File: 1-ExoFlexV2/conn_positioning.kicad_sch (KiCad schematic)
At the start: 39 parts, among them J47 3, J48 3, J49 3, J50 2, J51 2, J52 2, J53 4, J54 4, J55 4

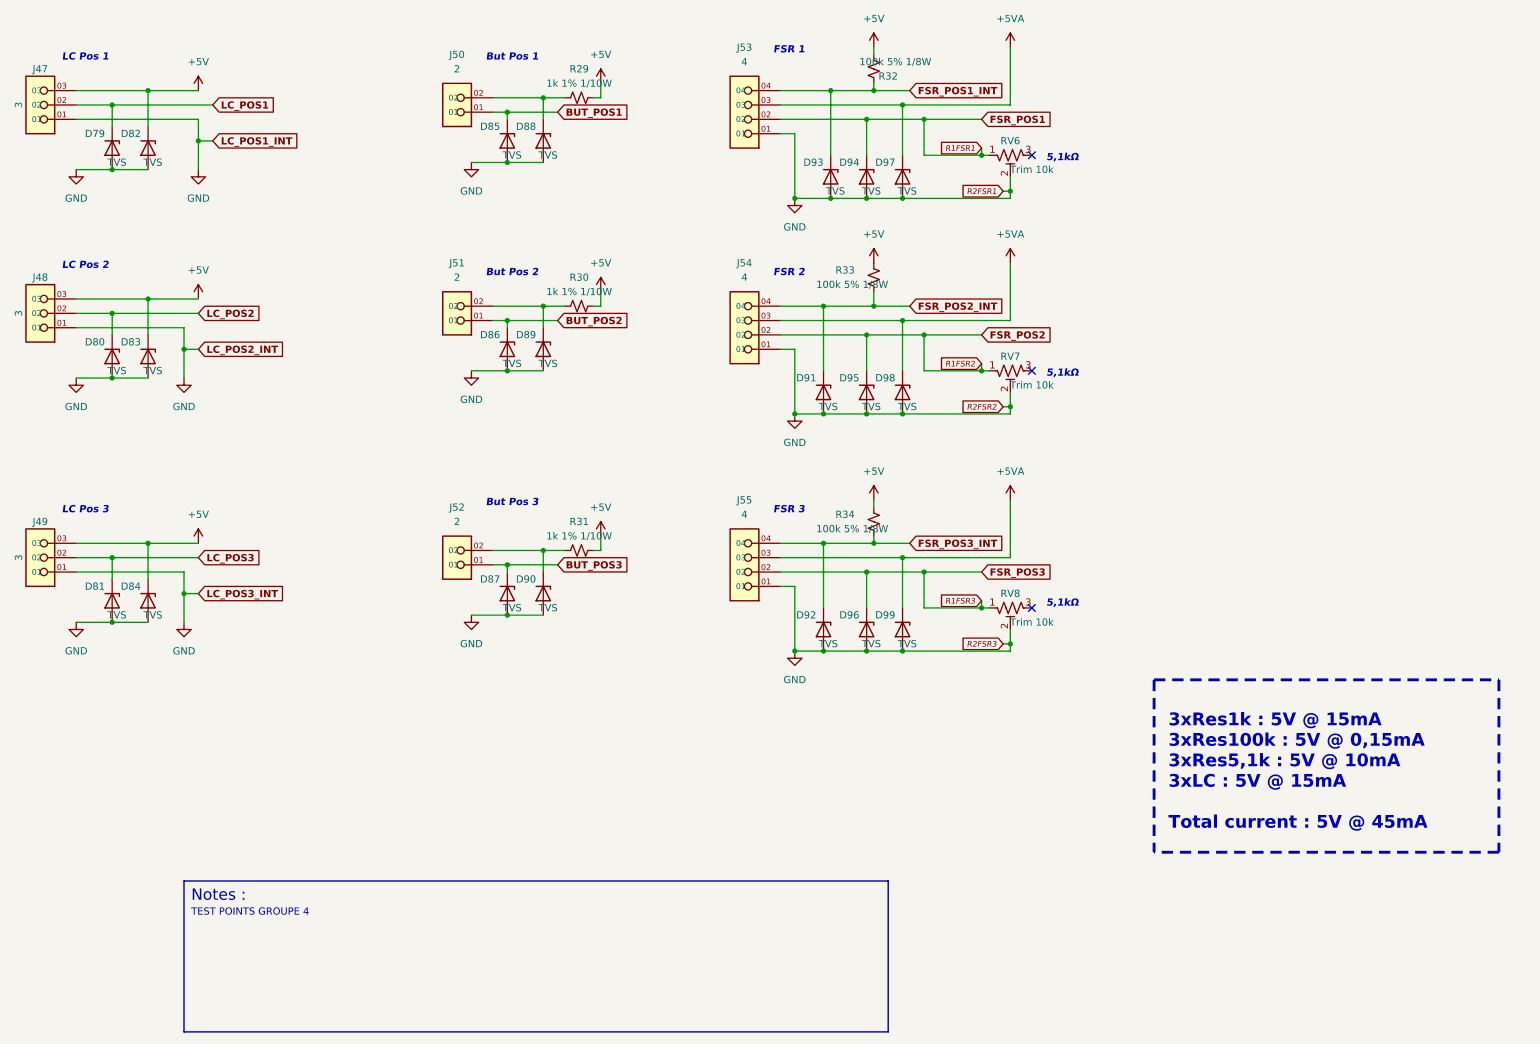
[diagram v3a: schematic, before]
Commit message: Bug NetList
- Ajout de net-tie pour les GND et et les +5V
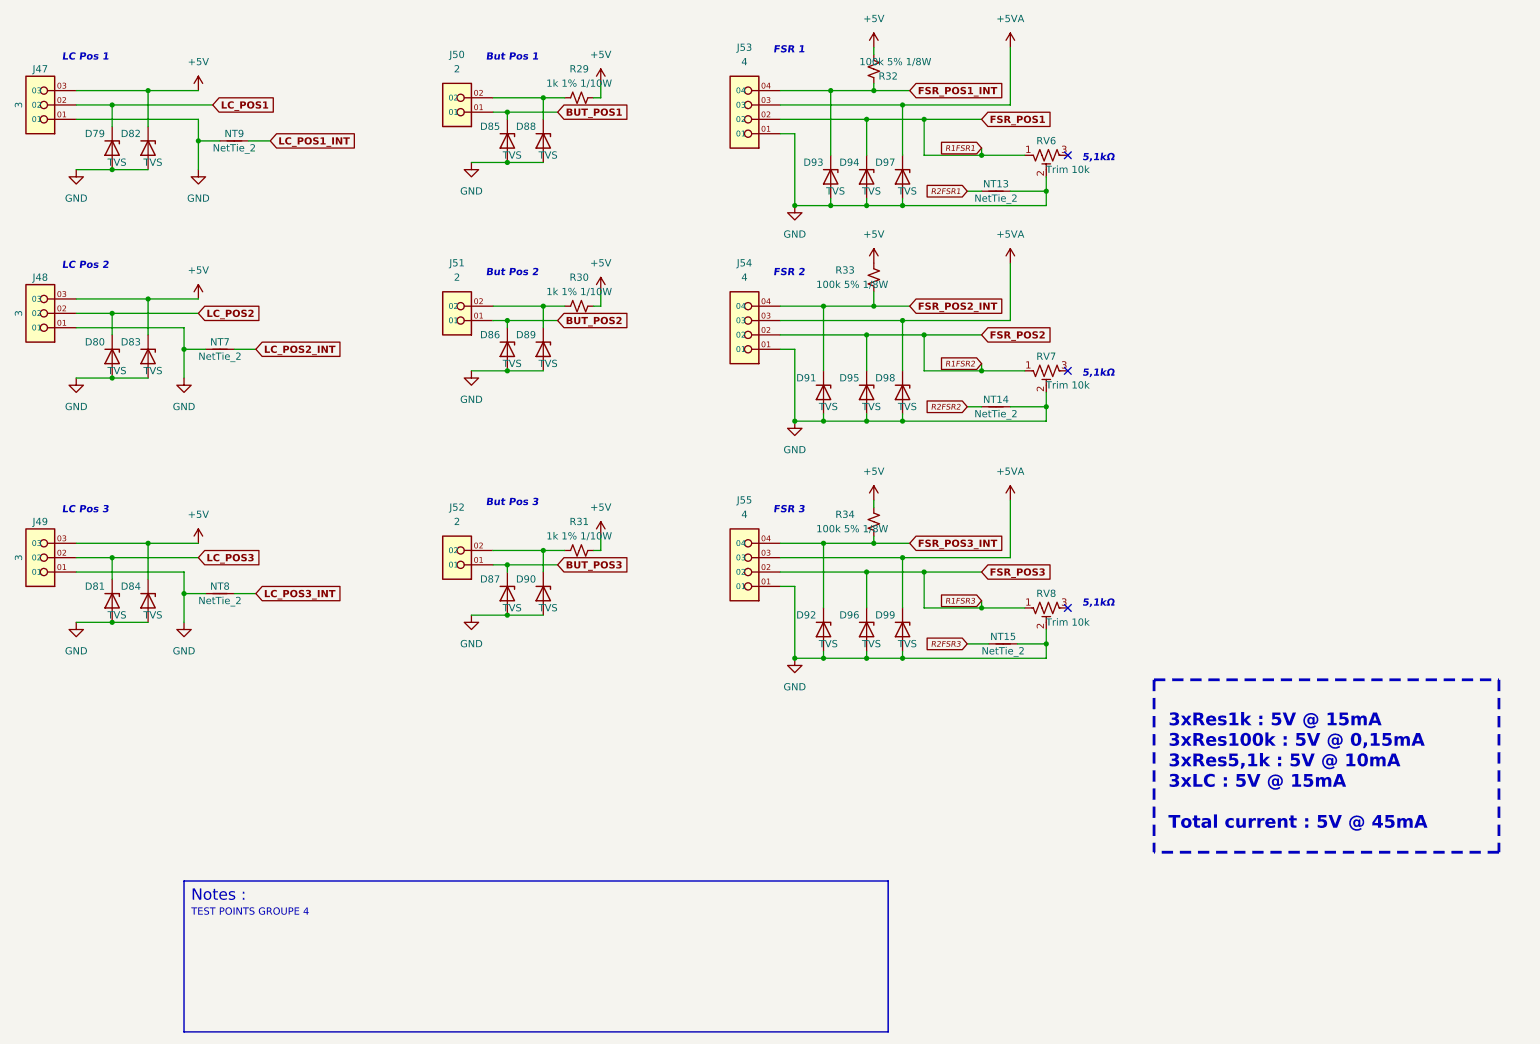
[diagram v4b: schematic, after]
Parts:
- added NT13, NT14, NT15, NT7, NT8, NT9: NetTie_2, NetTie:NetTie-2_SMD_Pad0.5mm, symbol Device:NetTie_2
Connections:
- net GND: now also NT13.2, NT14.2, NT15.2, NT7.1, NT8.1, NT9.1
- new net LC_POS1_INT: NT9.2
- new net LC_POS2_INT: NT7.2
- new net LC_POS3_INT: NT8.2
- new net R2FSR1: NT13.1
- new net R2FSR2: NT14.1
- new net R2FSR3: NT15.1
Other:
- moved on the sheet: RV6, RV7, RV8

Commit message: PLACEMENT 1
- Placement des connnecteurs
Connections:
- net +5V: no longer D82.1 (K), D83.1 (K), D84.1 (K), J47.03, J48.03, J49.03, R32.1, R33.1, R34.1
- net +5VA: now also D82.1 (K), D83.1 (K), D84.1 (K), J47.03, J48.03, J49.03, R32.1, R33.1, R34.1
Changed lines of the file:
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@@
     (pin "2")
-  )
-  (symbol (lib_id "power:+5V") (at 52.07 66.04 0) (unit 1)
-    (in_bom yes) (on_board yes) (fields_autoplaced)
-    (property "Reference" "#PWR0114" (id 0) (at 52.07 69.85 0)
-      (effects (font (size 1.27 1.27)) hide)
-    )
-    (property "Value" "+5V" (id 1) (at 52.07 60.96 0))
-    (property "Footprint" "" (id 2) (at 52.07 66.04 0)
-      (effects (font (size 1.27 1.27)) hide)
-    )
-    (property "Datasheet" "" (id 3) (at 52.07 66.04 0)
-      (effects (font (size 1.27 1.27)) hide)
-    )
-    (pin "1")
   )
   (symbol (lib_id "Device:NetTie_2") (at 194.31 127 0) (unit 1)
@@
     (pin "1")
   )
-  (symbol (lib_id "power:+5V") (at 52.07 29.21 0) (unit 1)
-    (in_bom yes) (on_board yes) (fields_autoplaced)
-    (property "Reference" "#PWR0112" (id 0) (at 52.07 33.02 0)
-      (effects (font (size 1.27 1.27)) hide)
-    )
-    (property "Value" "+5V" (id 1) (at 52.07 24.13 0))
-    (property "Footprint" "" (id 2) (at 52.07 29.21 0)
-      (effects (font (size 1.27 1.27)) hide)
-    )
-    (property "Datasheet" "" (id 3) (at 52.07 29.21 0)
-      (effects (font (size 1.27 1.27)) hide)
-    )
-    (pin "1")
-  )
   (symbol (lib_id "Device:D_Zener") (at 170.18 124.46 270) (unit 1)
     (in_bom yes) (on_board yes)
@@
     (pin "2")
   )
-  (symbol (lib_id "power:+5V") (at 52.07 109.22 0) (unit 1)
-    (in_bom yes) (on_board yes) (fields_autoplaced)
-    (property "Reference" "#PWR0115" (id 0) (at 52.07 113.03 0)
-      (effects (font (size 1.27 1.27)) hide)
-    )
-    (property "Value" "+5V" (id 1) (at 52.07 104.14 0))
-    (property "Footprint" "" (id 2) (at 52.07 109.22 0)
-      (effects (font (size 1.27 1.27)) hide)
-    )
-    (property "Datasheet" "" (id 3) (at 52.07 109.22 0)
+  (symbol (lib_id "power:+5VA") (at 171.45 59.69 0) (unit 1)
+    (in_bom yes) (on_board yes) (fields_autoplaced)
+    (property "Reference" "#PWR0126" (id 0) (at 171.45 63.5 0)
+      (effects (font (size 1.27 1.27)) hide)
+    )
+    (property "Value" "+5VA" (id 1) (at 171.45 54.61 0))
+    (property "Footprint" "" (id 2) (at 171.45 59.69 0)
+      (effects (font (size 1.27 1.27)) hide)
+    )
+    (property "Datasheet" "" (id 3) (at 171.45 59.69 0)
+      (effects (font (size 1.27 1.27)) hide)
+    )
+    (pin "1")
+  )
+  (symbol (lib_id "power:+5VA") (at 171.45 21.59 0) (unit 1)
+    (in_bom yes) (on_board yes) (fields_autoplaced)
+    (property "Reference" "#PWR0125" (id 0) (at 171.45 25.4 0)
+      (effects (font (size 1.27 1.27)) hide)
+    )
+    (property "Value" "+5VA" (id 1) (at 171.45 16.51 0))
+    (property "Footprint" "" (id 2) (at 171.45 21.59 0)
+      (effects (font (size 1.27 1.27)) hide)
+    )
+    (property "Datasheet" "" (id 3) (at 171.45 21.59 0)
       (effects (font (size 1.27 1.27)) hide)
     )
@@
     (pin "1")
     (pin "2")
+  )
+  (symbol (lib_id "power:+5VA") (at 52.07 66.04 0) (unit 1)
+    (in_bom yes) (on_board yes) (fields_autoplaced)
+    (property "Reference" "#PWR0114" (id 0) (at 52.07 69.85 0)
+      (effects (font (size 1.27 1.27)) hide)
+    )
+    (property "Value" "+5VA" (id 1) (at 52.07 60.96 0))
+    (property "Footprint" "" (id 2) (at 52.07 66.04 0)
+      (effects (font (size 1.27 1.27)) hide)
+    )
+    (property "Datasheet" "" (id 3) (at 52.07 66.04 0)
+      (effects (font (size 1.27 1.27)) hide)
+    )
+    (pin "1")
   )
   (symbol (lib_id "SymLib:1751112") (at 144.78 111.76 180) (unit 1)
@@
     (pin "1")
   )
-  (symbol (lib_id "power:+5V") (at 171.45 21.59 0) (unit 1)
-    (in_bom yes) (on_board yes) (fields_autoplaced)
-    (property "Reference" "#PWR0125" (id 0) (at 171.45 25.4 0)
-      (effects (font (size 1.27 1.27)) hide)
-    )
-    (property "Value" "+5V" (id 1) (at 171.45 16.51 0))
-    (property "Footprint" "" (id 2) (at 171.45 21.59 0)
-      (effects (font (size 1.27 1.27)) hide)
-    )
-    (property "Datasheet" "" (id 3) (at 171.45 21.59 0)
-      (effects (font (size 1.27 1.27)) hide)
-    )
-    (pin "1")
-  )
   (symbol (lib_id "Device:R_Potentiometer_Trim_US") (at 201.93 78.74 90) (mirror x) (unit 1)
     (in_bom yes) (on_board yes)
@@
     (pin "2")
   )
+  (symbol (lib_id "power:+5VA") (at 52.07 109.22 0) (unit 1)
+    (in_bom yes) (on_board yes) (fields_autoplaced)
+    (property "Reference" "#PWR0115" (id 0) (at 52.07 113.03 0)
+      (effects (font (size 1.27 1.27)) hide)
+    )
+    (property "Value" "+5VA" (id 1) (at 52.07 104.14 0))
+    (property "Footprint" "" (id 2) (at 52.07 109.22 0)
+      (effects (font (size 1.27 1.27)) hide)
+    )
+    (property "Datasheet" "" (id 3) (at 52.07 109.22 0)
+      (effects (font (size 1.27 1.27)) hide)
+    )
+    (pin "1")
+  )
   (symbol (lib_id "Device:D_Zener") (at 176.53 82.55 270) (unit 1)
     (in_bom yes) (on_board yes)
@@
     (pin "03")
     (pin "04")
+  )
+  (symbol (lib_id "power:+5VA") (at 52.07 29.21 0) (unit 1)
+    (in_bom yes) (on_board yes) (fields_autoplaced)
+    (property "Reference" "#PWR0112" (id 0) (at 52.07 33.02 0)
+      (effects (font (size 1.27 1.27)) hide)
+    )
+    (property "Value" "+5VA" (id 1) (at 52.07 24.13 0))
+    (property "Footprint" "" (id 2) (at 52.07 29.21 0)
+      (effects (font (size 1.27 1.27)) hide)
+    )
+    (property "Datasheet" "" (id 3) (at 52.07 29.21 0)
+      (effects (font (size 1.27 1.27)) hide)
+    )
+    (pin "1")
   )
   (symbol (lib_id "power:+5V") (at 123.19 27.94 0) (unit 1)
@@
     (pin "2")
   )
-  (symbol (lib_id "power:+5V") (at 171.45 59.69 0) (unit 1)
-    (in_bom yes) (on_board yes) (fields_autoplaced)
-    (property "Reference" "#PWR0126" (id 0) (at 171.45 63.5 0)
-      (effects (font (size 1.27 1.27)) hide)
-    )
-    (property "Value" "+5V" (id 1) (at 171.45 54.61 0))
-    (property "Footprint" "" (id 2) (at 171.45 59.69 0)
-      (effects (font (size 1.27 1.27)) hide)
-    )
-    (property "Datasheet" "" (id 3) (at 171.45 59.69 0)
+  (symbol (lib_id "power:+5VA") (at 171.45 101.6 0) (unit 1)
+    (in_bom yes) (on_board yes) (fields_autoplaced)
+    (property "Reference" "#PWR0127" (id 0) (at 171.45 105.41 0)
+      (effects (font (size 1.27 1.27)) hide)
+    )
+    (property "Value" "+5VA" (id 1) (at 171.45 96.52 0))
+    (property "Footprint" "" (id 2) (at 171.45 101.6 0)
+      (effects (font (size 1.27 1.27)) hide)
+    )
+    (property "Datasheet" "" (id 3) (at 171.45 101.6 0)
       (effects (font (size 1.27 1.27)) hide)
     )
@@
     (in_bom yes) (on_board yes)
     (property "Reference" "R32" (id 0) (at 173.99 26.67 0))
-    (property "Value" "100k 5% 1/8W" (id 1) (at 175.26 24.13 0))
+    (property "Value" "100k 5% 1/8W" (id 1) (at 179.07 24.13 0))
     (property "Footprint" "Resistor_SMD:R_0805_2012Metric" (id 2) (at 171.45 25.4 0)
       (effects (font (size 1.27 1.27)) hide)
@@
     (pin "2")
   )
-  (symbol (lib_id "power:+5V") (at 171.45 101.6 0) (unit 1)
-    (in_bom yes) (on_board yes) (fields_autoplaced)
-    (property "Reference" "#PWR0127" (id 0) (at 171.45 105.41 0)
-      (effects (font (size 1.27 1.27)) hide)
-    )
-    (property "Value" "+5V" (id 1) (at 171.45 96.52 0))
-    (property "Footprint" "" (id 2) (at 171.45 101.6 0)
-      (effects (font (size 1.27 1.27)) hide)
-    )
-    (property "Datasheet" "" (id 3) (at 171.45 101.6 0)
-      (effects (font (size 1.27 1.27)) hide)
-    )
-    (pin "1")
-  )
   (symbol (lib_id "power:GND") (at 157.48 49.53 0) (unit 1)
